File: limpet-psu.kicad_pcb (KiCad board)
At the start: 2 copper layers, 27 x 18 mm, 16 parts, among them J1 USB_C_Receptacle_HRO_TYPE-C-3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, U1 RT6154AGQW

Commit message: output
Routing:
- net +3V3: track 5.12 -> 0.25 mm
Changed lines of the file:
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@@
   (via (at 195.5 77.4) (size 0.5) (drill 0.3) (layers "F.Cu" "B.Cu") (free) (net 1))
   (segment (start 204.1 80.45) (end 204.275 80.625) (width 0.4) (layer "F.Cu") (net 4))
-  (segment (start 207 84.95) (end 207 81.35) (width 1) (layer "F.Cu") (net 4))
-  (segment (start 207 81.35) (end 206.1 80.45) (width 1) (layer "F.Cu") (net 4))
   (segment (start 188.95 81.139004) (end 188.95 76.95) (width 0.4) (layer "F.Cu") (net 5))
   (segment (start 190.045 81.45) (end 189.260996 81.45) (width 0.4) (layer "F.Cu") (net 5))
@@
     (polygon
       (pts
-        (xy 203.925 81.825)
-        (xy 201.1 81.825)
+        (xy 203.85 81.85)
+        (xy 201.1 81.85)
         (xy 201.1 81.375)
-        (xy 203.925 81.375)
+        (xy 203.85 81.375)
       )
     )
@@
     (polygon
       (pts
-        (xy 211 90)
-        (xy 168.55 90)
-        (xy 168.55 68)
-        (xy 211 68)
+        (xy 211 89)
+        (xy 181 89)
+        (xy 181 69)
+        (xy 211 69)
       )
     )

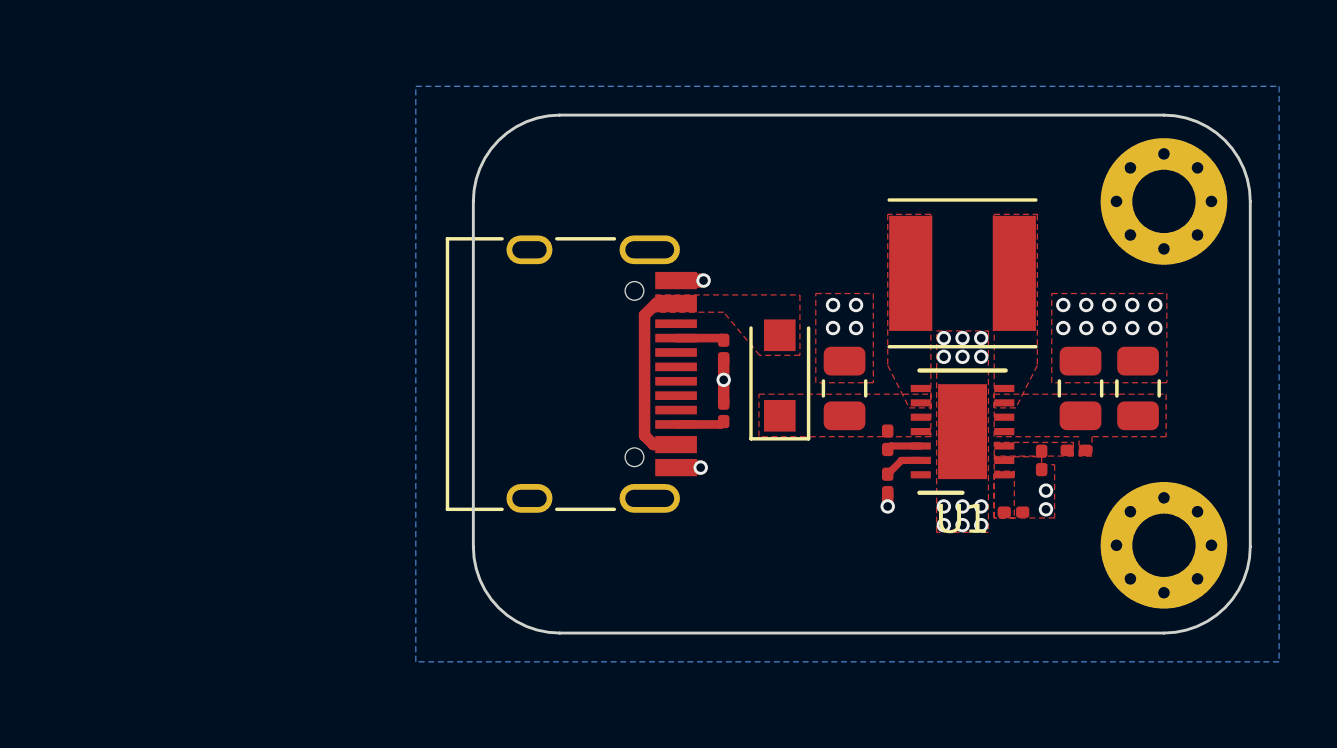
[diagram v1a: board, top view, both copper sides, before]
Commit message: zones cleaned
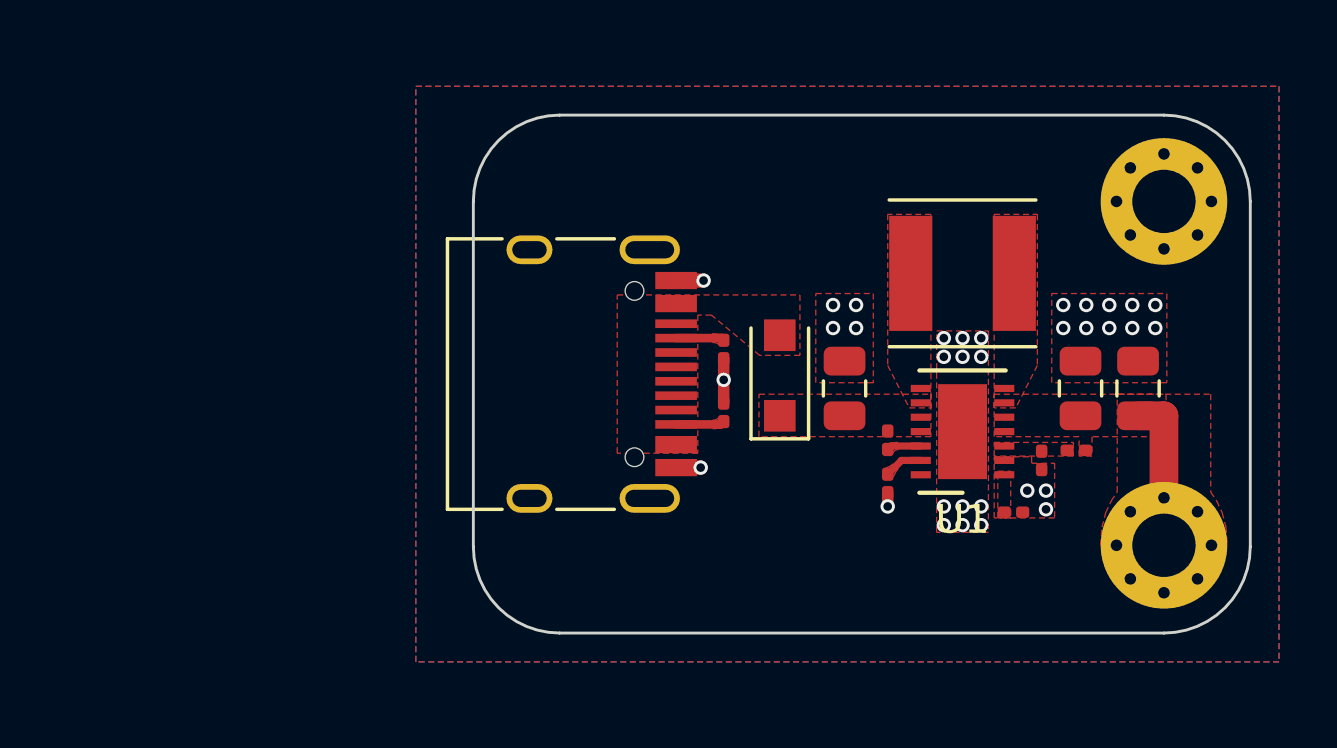
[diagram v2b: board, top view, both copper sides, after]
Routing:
- net VBUS: track 6.67 -> 0.00 mm
- net +3V3: track 0.25 -> 5.65 mm
- net GND: vias 32 -> 33

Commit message: 2ndary
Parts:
- added Q1: AO3401A, Package_TO_SOT_SMD:SOT-23, F.Cu at (194.6, 75.6)
- D1: value D_Schottky_Small -> 3A 200V
- L1: value L_Small -> 3u3 4.5A
- R1, R2: value 100K -> 5K1
- moved C1 1.90 mm to (195.9, 81.4), turned to 90 degrees
- moved D1 0.79 mm to (194.4, 78.8), turned to 180 degrees
- moved J1 0.32 mm to (185.7, 79.0)
- moved R1 0.32 mm to (191.4, 80.3)
- moved R2 0.32 mm to (191.4, 78.1)
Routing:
- net +3V3: track 5.65 -> 0.25 mm
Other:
- board size 27 x 18 mm -> 24.9 x 18 mm
